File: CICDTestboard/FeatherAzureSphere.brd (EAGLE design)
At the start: 64.4 x 72.4 mm, 7 parts

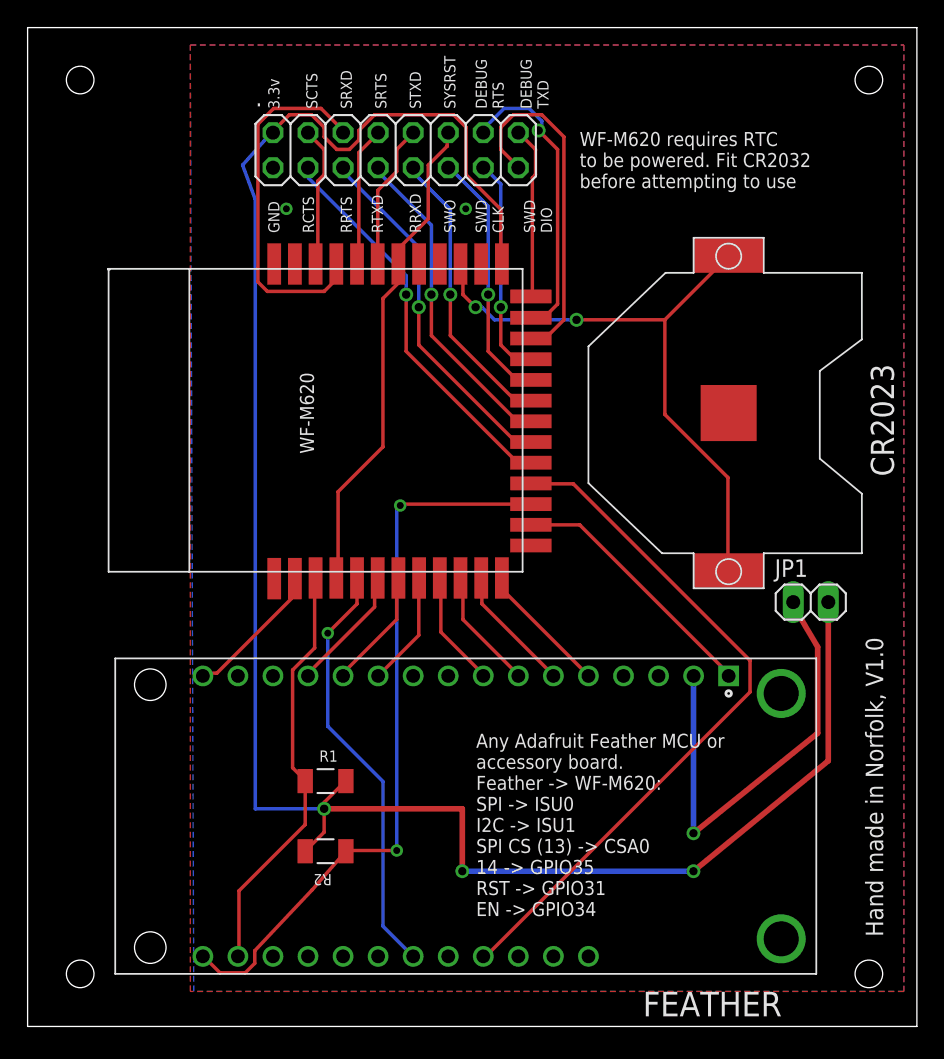
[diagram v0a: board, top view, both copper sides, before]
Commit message: Correction of RSC1 module footprint
The RSC1 footprint was flawed and has been corrected. Impacted board updated.
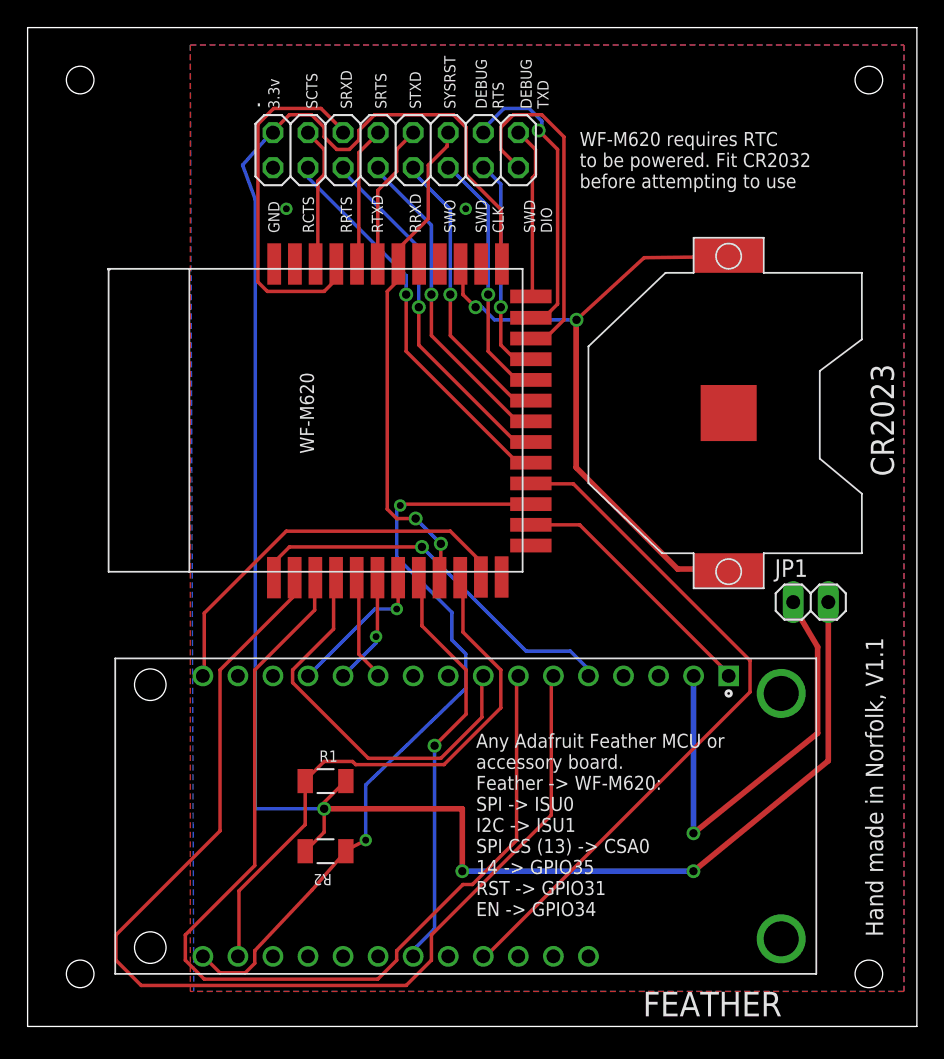
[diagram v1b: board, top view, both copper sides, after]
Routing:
- net ADC1: track 9.26 -> 81.8 mm
- net ADC2: track 8.89 -> 72.8 mm
- net ADC3: track 8.40 -> 29.3 mm
- net FEATHER_ENABLE: track 10.3 -> 29.1 mm
- net ADC: track 9.74 -> 28.5 mm, vias 0 -> 1
- net SCL: track 30.5 -> 42.0 mm
- net RTC_V3: track 44.4 -> 49.0 mm
- net SDA: track 53.8 -> 56.1 mm
- net MISO: track 9.28 -> 10.7 mm, vias 0 -> 1
- net SYSRST_N: track 35.6 -> 36.5 mm, vias 0 -> 2
- net MOSI: track 8.80 -> 8.15 mm, vias 0 -> 1
- net SCK: track 8.33 -> 7.79 mm
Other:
- board text added: "Hand made in Norfolk, V1.1"
- board text removed: "Hand made in Norfolk, V1.0"
